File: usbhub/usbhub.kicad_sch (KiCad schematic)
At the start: 44 parts, among them J1 USB_A, J2 USB_A, J3 USB_InputPort, J4 USB_A, J5 USB_InputPort, J6 USB_A, J7 Conn_01x05_Male, J8 Power, J9 Power, U1 FE1.1s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

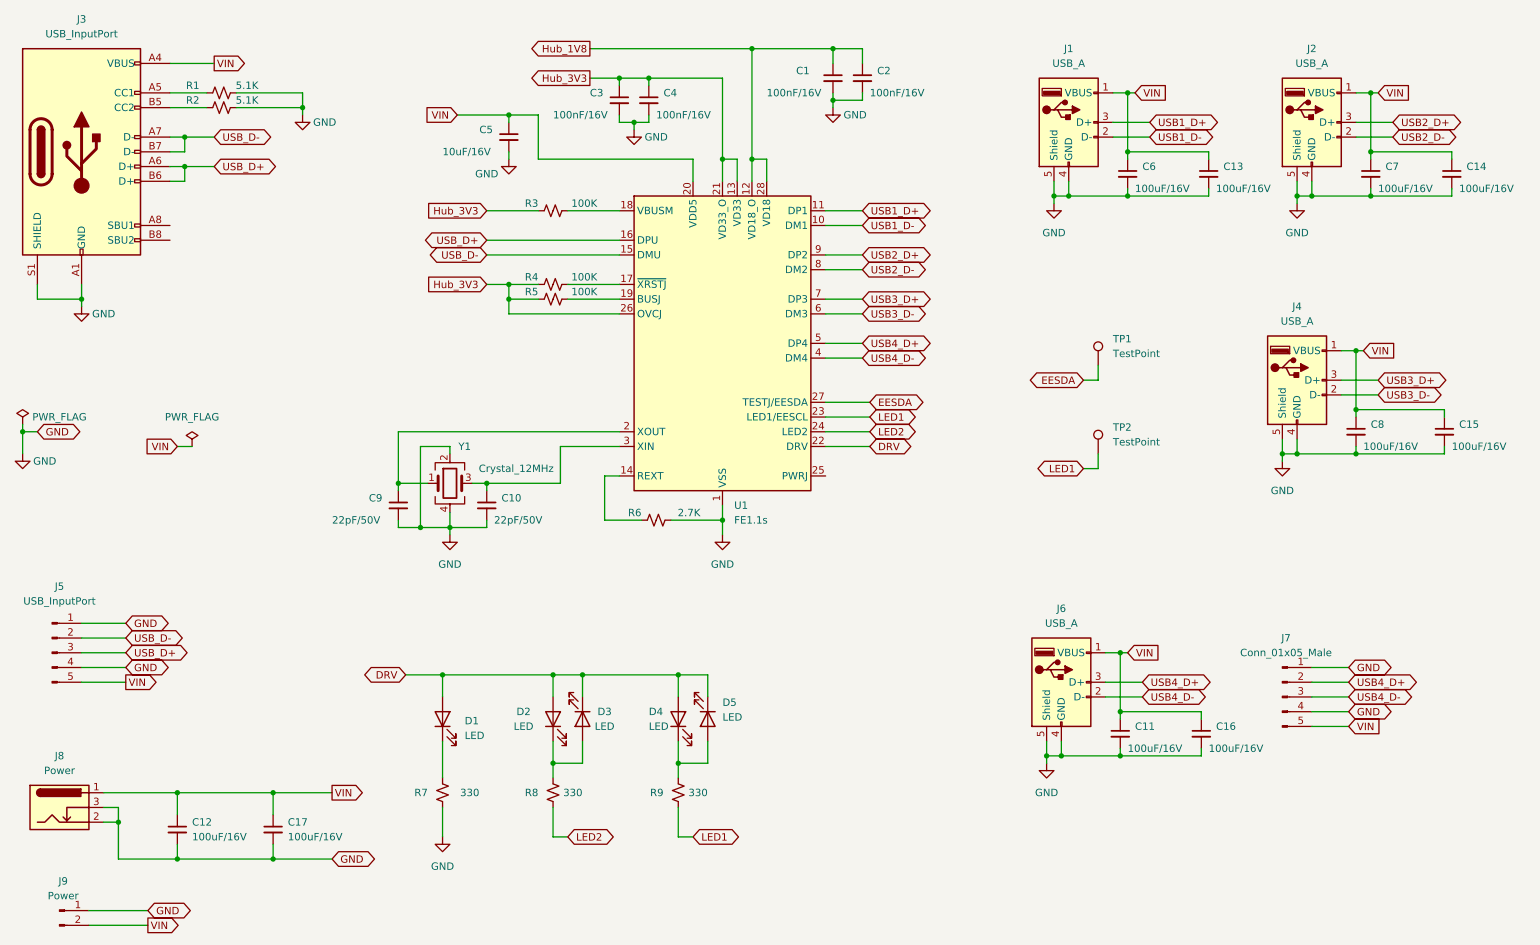
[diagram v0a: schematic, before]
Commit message: change usb2.0 hub board design
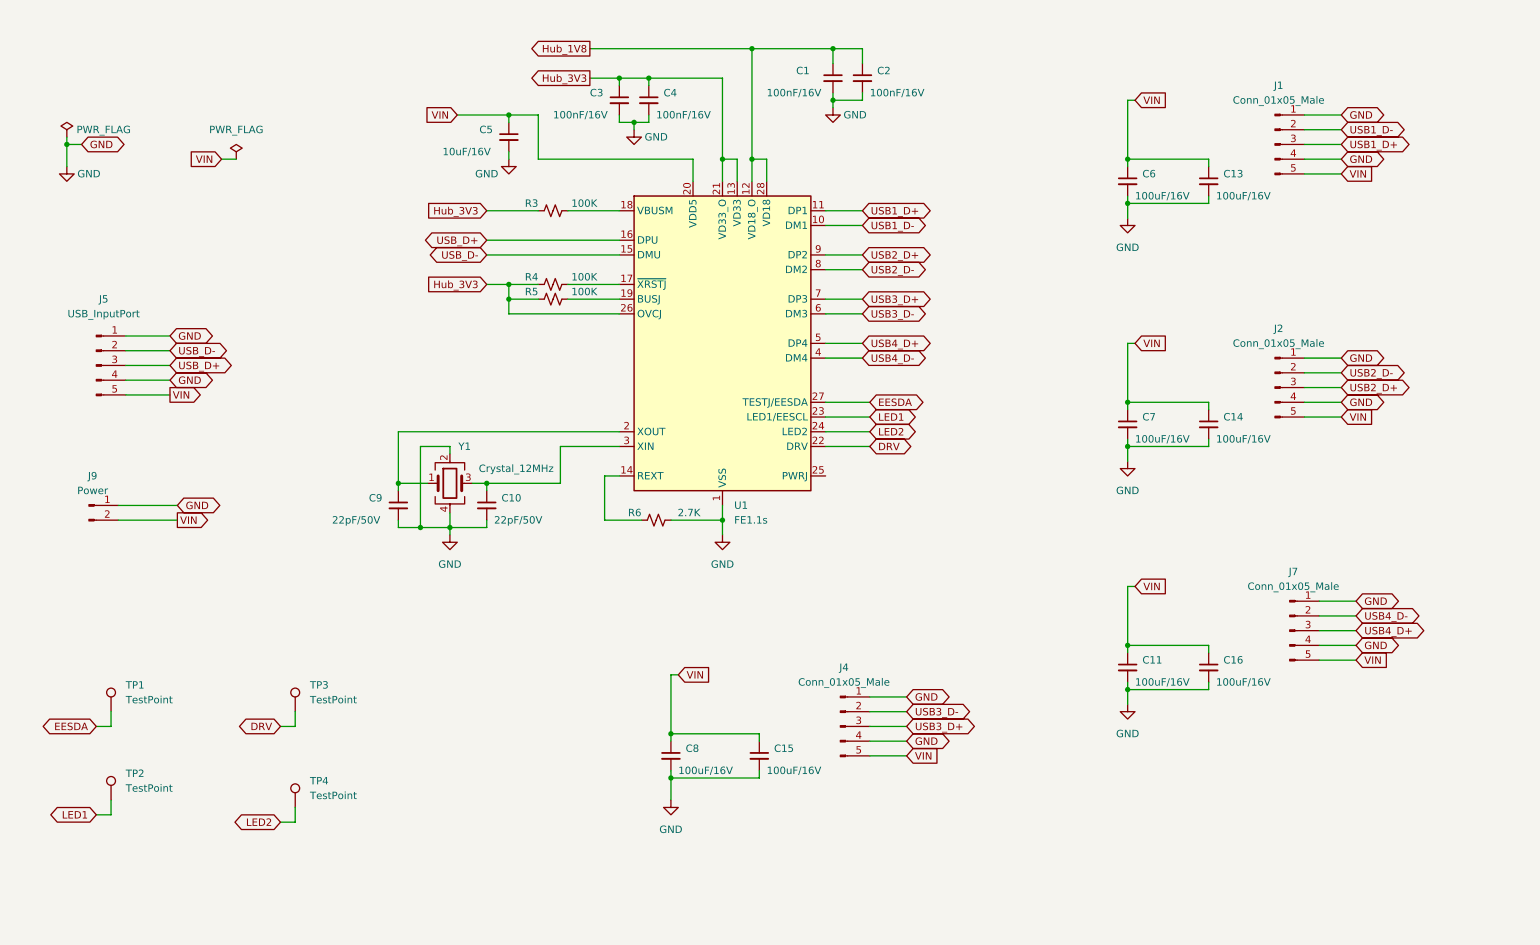
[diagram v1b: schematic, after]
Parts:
- removed C12: 100uF/16V, Capacitor_SMD:C_1206_3216Metric, symbol Device:C_Small
- removed C17: 100uF/16V, Capacitor_SMD:C_0603_1608Metric, symbol Device:C_Small
- removed D1, D2, D3, D4, D5: LED, LED_SMD:LED_0603_1608Metric, symbol Device:LED
- removed J1, J2, J4, J6: USB_A, Connector_USB:USB_A_TE_292303-7_Horizontal, symbol Connector:USB_A
- removed J3: USB_InputPort, Connector_USB:USB_C_Receptacle_HRO_TYPE-C-31-M-12, symbol Connector:USB_C_Receptacle_USB2.0
- removed J8: Power, Connector_BarrelJack:BarrelJack_Horizontal, symbol Connector:Barrel_Jack_Switch
- removed R1, R2: 5.1K, Resistor_SMD:R_0603_1608Metric, symbol Device:R_Small_US
- removed R7, R8, R9: 330, Resistor_SMD:R_0603_1608Metric, symbol Device:R_Small_US
- added J1, J2, J4: Conn_01x05_Male, Connector_Molex:Molex_PicoBlade_53261-0571_1x05-1MP_P1.25mm_Horizontal, symbol Connector:Conn_01x05_Male
- added TP3, TP4: TestPoint, TestPoint:TestPoint_Pad_D1.0mm, symbol Connector:TestPoint
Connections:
- net DRV: now also TP3.1
- net GND: now also J1.1 (Pin_1), J1.4 (Pin_4), J2.1 (Pin_1), J2.4 (Pin_4), J4.1 (Pin_1), J4.4 (Pin_4)
- net LED2: now also TP4.1
- net USB1_D+: now also J1.3 (Pin_3)
- net USB1_D-: now also J1.2 (Pin_2)
- net USB2_D+: now also J2.3 (Pin_3)
- net USB2_D-: now also J2.2 (Pin_2)
- net USB3_D+: now also J4.3 (Pin_3)
- net USB3_D-: now also J4.2 (Pin_2)
- net USB4_D+: now also J7.3 (Pin_3); no longer J7.2 (Pin_2)
- net USB4_D-: now also J7.2 (Pin_2); no longer J7.3 (Pin_3)
- net VIN: now also J1.5 (Pin_5), J2.5 (Pin_5), J4.5 (Pin_5)
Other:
- moved on the sheet: C11, C13, C14, C15, C16, C6, C7, C8, J5, J7, J9, TP1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
